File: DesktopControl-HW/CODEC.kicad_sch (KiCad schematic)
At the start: 16 parts, among them U201 PCM2902, Y201 LFXTAL035264

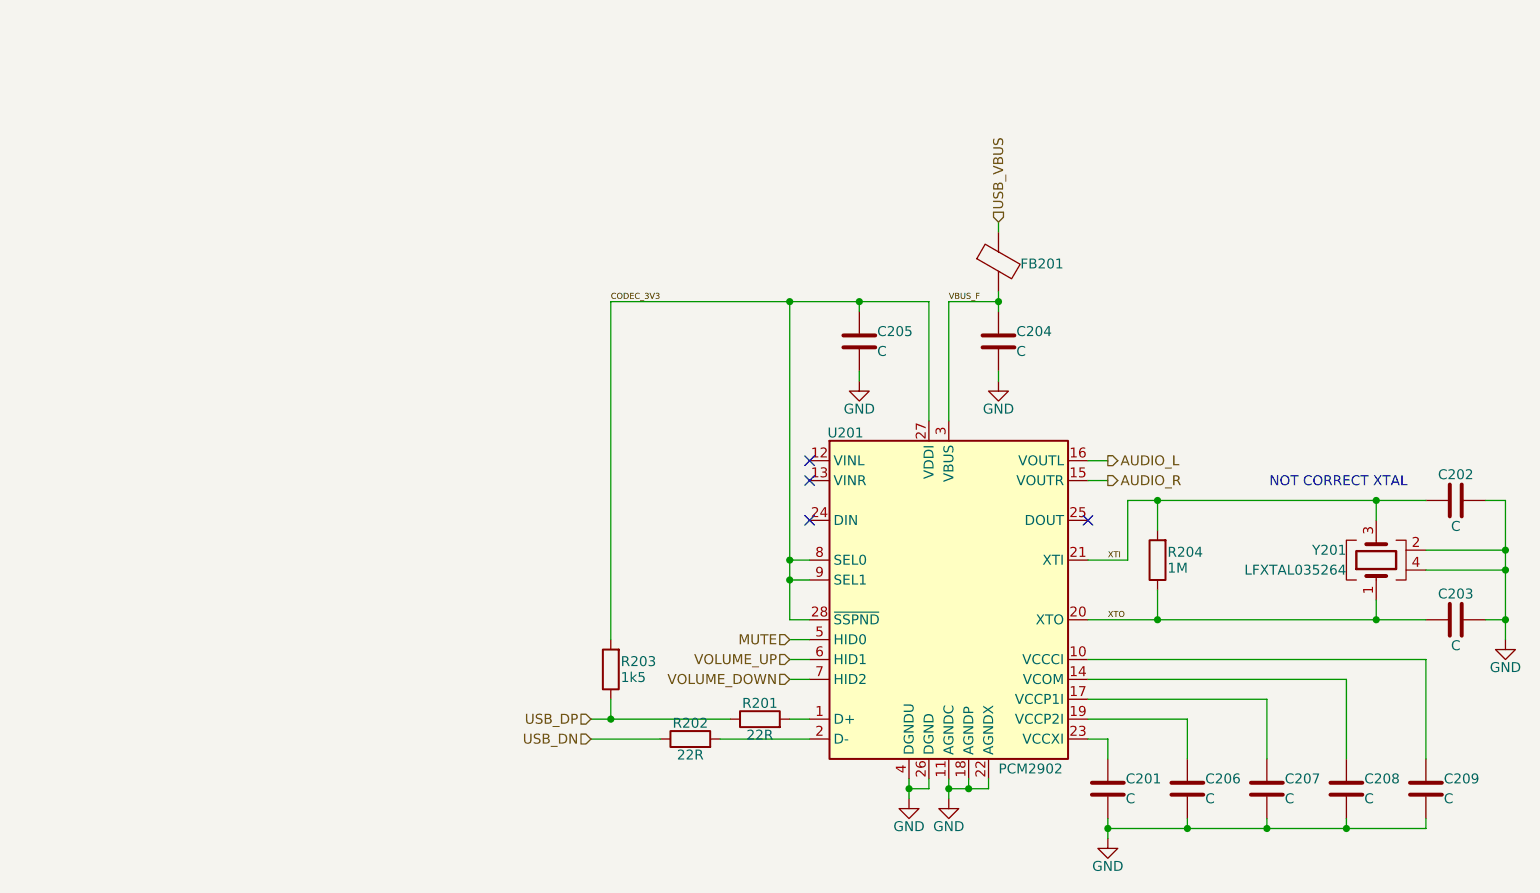
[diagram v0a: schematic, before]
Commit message: Rework amplifier configuration, add amplifier for subwoofer and start check of codec
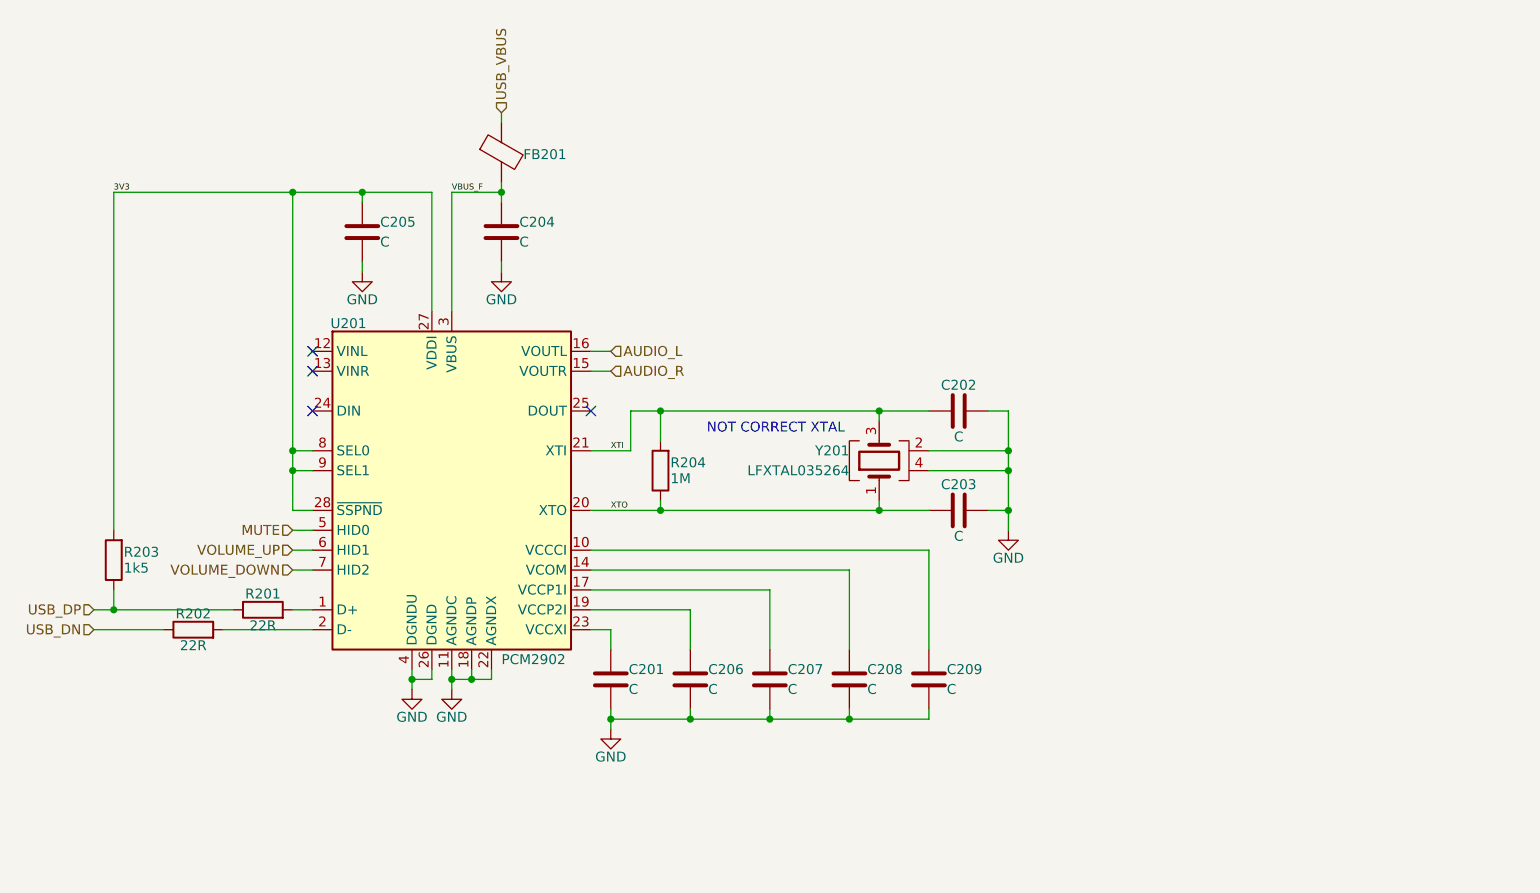
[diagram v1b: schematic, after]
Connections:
- net CODEC_3V3 renamed 3V3
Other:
- moved on the sheet: C201, C202, C203, C204, C205, C206, C207, C208, C209, FB201, R201, R202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
